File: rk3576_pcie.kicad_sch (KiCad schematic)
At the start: 5 parts, among them U27 RK3576

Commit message: Add files via upload
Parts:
- renumbered C261 to C159, C263 to C160, C320 to C161, C324 to C162, U27 to U2

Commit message: SBC Board V0.2
The SBC schematics before footprint and part number check
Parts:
- U3: renamed from U2; footprint (none) -> easyeda2kicad:FCCSP-698_L17.2-W16.1-TL_RK3576
- renumbered C159 to C167, C160 to C168, C161 to C169, C162 to C170

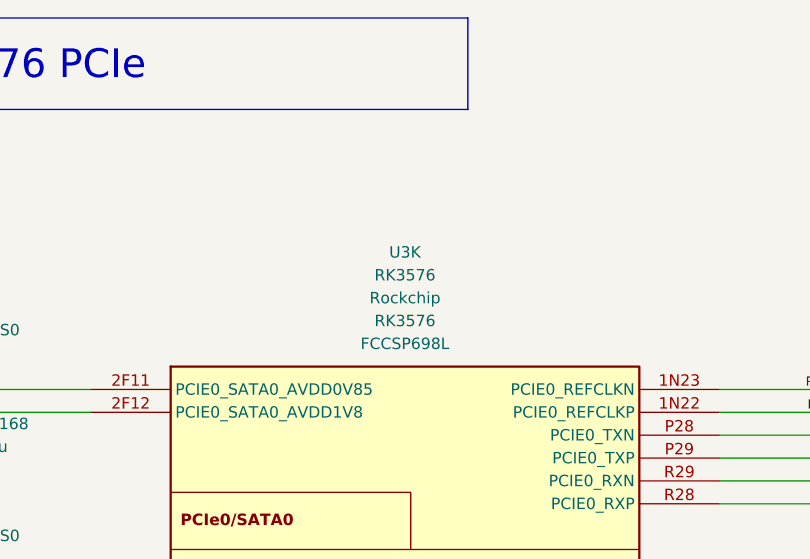
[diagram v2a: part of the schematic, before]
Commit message: SBCv0.3
there is no big thing update just some LCSC & Mouser parts
and Big problem deleted alot of component values (:
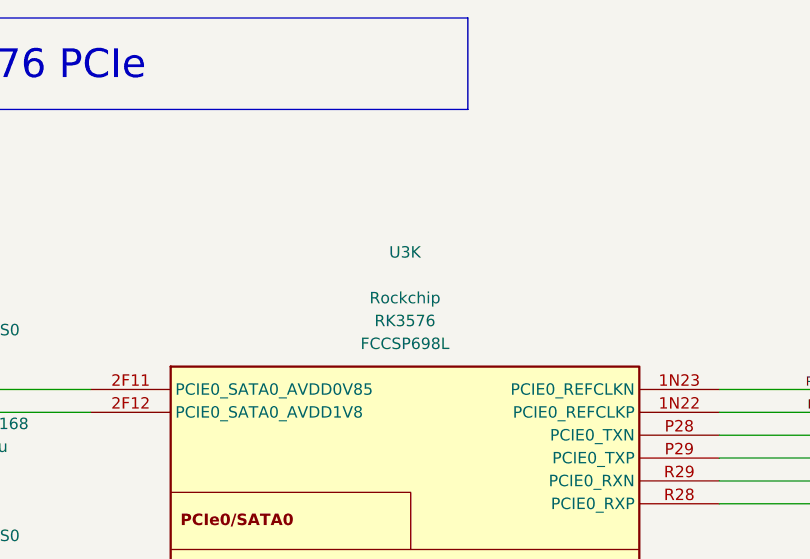
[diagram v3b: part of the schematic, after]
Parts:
- C167, C168, C169, C170: footprint Capacitor_SMD:C_0402_1005Metric_Pad0.74x0.62mm_HandSolder -> Capacitor_SMD:C_0201_0603Metric_Pad0.64x0.40mm_HandSolder; LCSC Part (none) -> C5209398; Mouser Part (none) -> CL03A105KP3NSNC
- U3: value RK3576 -> (none); LCSC Part (none) -> (polyline
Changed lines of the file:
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@@
 			)
 		)
-		(property "Footprint" "Capacitor_SMD:C_0402_1005Metric_Pad0.74x0.62mm_HandSolder"
+		(property "Footprint" "Capacitor_SMD:C_0201_0603Metric_Pad0.64x0.40mm_HandSolder"
 			(at 55.88 58.42 0)
 			(hide yes)
@@
 			)
 		)
-		(property "KLC_S5.1" ""
+		(property "LCSC Part" "C5209398"
+			(at 55.88 58.42 0)
+			(hide yes)
+			(show_name no)
+			(do_not_autoplace no)
+			(effects
+				(font
+					(size 1.27 1.27)
+				)
+			)
+		)
+		(property "Mouser Part" "CL03A105KP3NSNC "
+			(at 55.88 58.42 0)
+			(hide yes)
+			(show_name no)
+			(do_not_autoplace no)
+			(effects
+				(font
+					(size 1.27 1.27)
+				)
+			)
+		)
+		(property "KLC_S4.2_DVDD" ""
+			(at 55.88 58.42 0)
+			(hide yes)
+			(show_name no)
+			(do_not_autoplace no)
+			(effects
+				(font
+					(size 1.27 1.27)
+				)
+			)
+		)
+		(property "KLC_S4.2_VREG_LX" ""
 			(at 55.88 58.42 0)
 			(hide yes)
@@
 					(reference "C168")
 					(unit 1)
+					(variant
+						(name "Test")
+					)
 				)
 			)
@@
 			)
 		)
-		(property "Footprint" "Capacitor_SMD:C_0402_1005Metric_Pad0.74x0.62mm_HandSolder"
+		(property "Footprint" "Capacitor_SMD:C_0201_0603Metric_Pad0.64x0.40mm_HandSolder"
 			(at 40.64 58.42 0)
 			(hide yes)
@@
 			)
 		)
-		(property "KLC_S5.1" ""
+		(property "LCSC Part" "C5209398"
+			(at 40.64 58.42 0)
+			(hide yes)
+			(show_name no)
+			(do_not_autoplace no)
+			(effects
+				(font
+					(size 1.27 1.27)
+				)
+			)
+		)
+		(property "Mouser Part" "CL03A105KP3NSNC "
+			(at 40.64 58.42 0)
+			(hide yes)
+			(show_name no)
+			(do_not_autoplace no)
+			(effects
+				(font
+					(size 1.27 1.27)
+				)
+			)
+		)
+		(property "KLC_S4.2_DVDD" ""
+			(at 40.64 58.42 0)
+			(hide yes)
+			(show_name no)
+			(do_not_autoplace no)
+			(effects
+				(font
+					(size 1.27 1.27)
+				)
+			)
+		)
+		(property "KLC_S4.2_VREG_LX" ""
 			(at 40.64 58.42 0)
 			(hide yes)
@@
 					(reference "C167")
 					(unit 1)
+					(variant
+						(name "Test")
+					)
 				)
 			)
@@
 			)
 		)
-		(property "Value" "RK3576"
+		(property "Value" ""
 			(at 104.775 40.64 0)
 			(show_name no)
@@
 			)
 		)
-		(property "KLC_S5.1" ""
+		(property "LCSC Part" "(polyline"
+			(at 105.41 71.12 0)
+			(hide yes)
+			(show_name no)
+			(do_not_autoplace no)
+			(effects
+				(font
+					(size 1.27 1.27)
+				)
+			)
+		)
+		(property "KLC_S4.2_DVDD" ""
+			(at 105.41 71.12 0)
+			(hide yes)
+			(show_name no)
+			(do_not_autoplace no)
+			(effects
+				(font
+					(size 1.27 1.27)
+				)
+			)
+		)
+		(property "KLC_S4.2_VREG_LX" ""
 			(at 105.41 71.12 0)
 			(hide yes)
@@
 					(reference "U3")
 					(unit 11)
+					(variant
+						(name "Test")
+					)
 				)
 			)
@@
 			)
 		)
-		(property "Footprint" "Capacitor_SMD:C_0402_1005Metric_Pad0.74x0.62mm_HandSolder"
+		(property "Footprint" "Capacitor_SMD:C_0201_0603Metric_Pad0.64x0.40mm_HandSolder"
 			(at 40.64 81.28 0)
 			(hide yes)
@@
 			)
 		)
-		(property "KLC_S5.1" ""
+		(property "LCSC Part" "C5209398"
+			(at 40.64 81.28 0)
+			(hide yes)
+			(show_name no)
+			(do_not_autoplace no)
+			(effects
+				(font
+					(size 1.27 1.27)
+				)
+			)
+		)
+		(property "Mouser Part" "CL03A105KP3NSNC "
+			(at 40.64 81.28 0)
+			(hide yes)
+			(show_name no)
+			(do_not_autoplace no)
+			(effects
+				(font
+					(size 1.27 1.27)
+				)
+			)
+		)
+		(property "KLC_S4.2_DVDD" ""
+			(at 40.64 81.28 0)
+			(hide yes)
+			(show_name no)
+			(do_not_autoplace no)
+			(effects
+				(font
+					(size 1.27 1.27)
+				)
+			)
+		)
+		(property "KLC_S4.2_VREG_LX" ""
 			(at 40.64 81.28 0)
 			(hide yes)
@@
 					(reference "C169")
 					(unit 1)
+					(variant
+						(name "Test")
+					)
 				)
 			)
@@
 			)
 		)
-		(property "Footprint" "Capacitor_SMD:C_0402_1005Metric_Pad0.74x0.62mm_HandSolder"
+		(property "Footprint" "Capacitor_SMD:C_0201_0603Metric_Pad0.64x0.40mm_HandSolder"
 			(at 55.88 81.28 0)
 			(hide yes)
@@
 			)
 		)
-		(property "KLC_S5.1" ""
+		(property "LCSC Part" "C5209398"
+			(at 55.88 81.28 0)
+			(hide yes)
+			(show_name no)
+			(do_not_autoplace no)
+			(effects
+				(font
+					(size 1.27 1.27)
+				)
+			)
+		)
+		(property "Mouser Part" "CL03A105KP3NSNC "
+			(at 55.88 81.28 0)
+			(hide yes)
+			(show_name no)
+			(do_not_autoplace no)
+			(effects
+				(font
+					(size 1.27 1.27)
+				)
+			)
+		)
+		(property "KLC_S4.2_DVDD" ""
+			(at 55.88 81.28 0)
+			(hide yes)
+			(show_name no)
+			(do_not_autoplace no)
+			(effects
+				(font
+					(size 1.27 1.27)
+				)
+			)
+		)
+		(property "KLC_S4.2_VREG_LX" ""
 			(at 55.88 81.28 0)
 			(hide yes)
@@
 					(reference "C170")
 					(unit 1)
-				)
-			)
+					(variant
+						(name "Test")
+					)
+				)
+			)

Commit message: SBCv0.4
add LCSC & Mouser parts 
and solve the deleted value in the past version
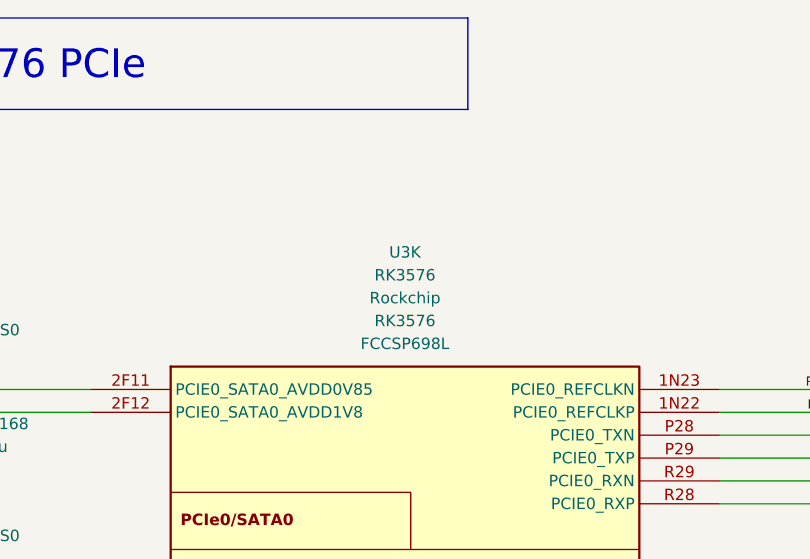
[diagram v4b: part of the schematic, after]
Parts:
- U3: value (none) -> RK3576; LCSC Part (polyline -> C42388007
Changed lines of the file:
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@@
 			)
 		)
-		(property "Value" ""
+		(property "Value" "RK3576"
 			(at 104.775 40.64 0)
 			(show_name no)
@@
 			)
 		)
-		(property "LCSC Part" "(polyline"
+		(property "LCSC Part" "C42388007"
 			(at 105.41 71.12 0)
 			(hide yes)
